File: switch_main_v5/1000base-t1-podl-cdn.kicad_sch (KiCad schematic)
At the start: 11 parts, among them T1901 74930100

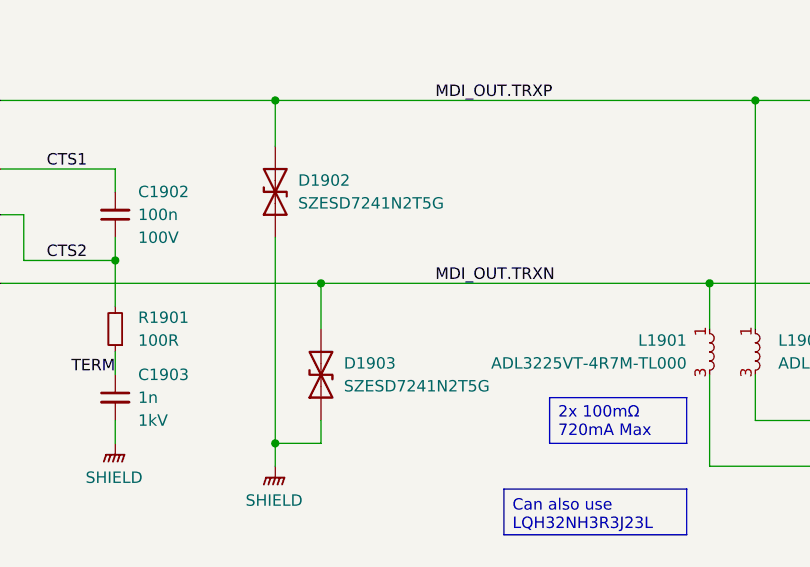
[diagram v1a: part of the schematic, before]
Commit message: Changed main 3V3 regulator to 3A, added switch 2 crystal & other changes
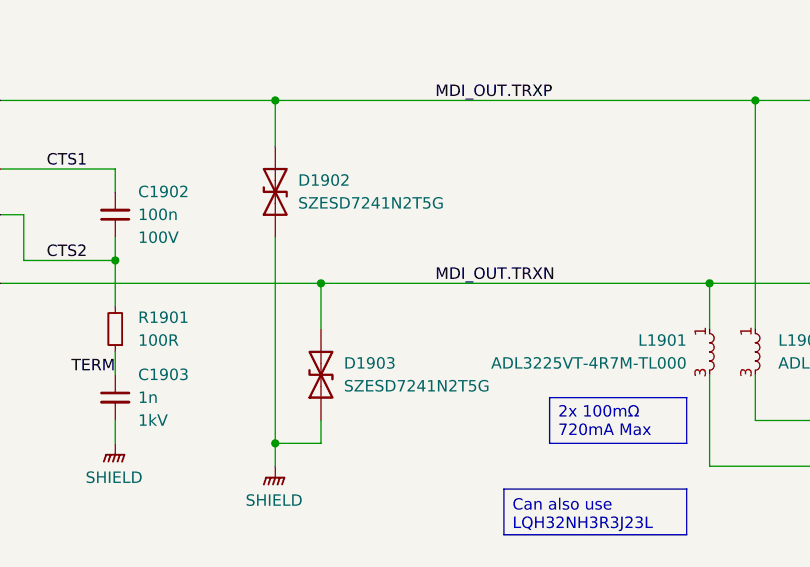
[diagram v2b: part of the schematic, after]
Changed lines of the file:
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@@
 	(symbol
 		(lib_id "TVS:SZESD7241N2T5G")
-		(at 177.8 124.46 90)
+		(at 180.34 124.46 90)
 		(unit 1)
 		(exclude_from_sim no)
@@
 		(on_board yes)
 		(dnp no)
-		(fields_autoplaced yes)
 		(property "Reference" "D1903"
-			(at 182.88 123.1899 90)
+			(at 182.88 123.19 90)
 			(effects
 				(font
@@
 		)
 		(property "Value" "SZESD7241N2T5G"
-			(at 182.88 125.7299 90)
+			(at 182.88 125.73 90)
 			(effects
 				(font
@@
 		)
 		(property "Footprint" "project_footprints:SZESD7462N2T5G"
-			(at 187.96 140.97 0)
+			(at 190.5 140.97 0)
 			(effects
 				(font
@@
 		)
 		(property "Datasheet" "https://www.onsemi.com/pub/Collateral/ESD7241-D.PDF"
-			(at 190.5 153.67 0)
+			(at 193.04 153.67 0)
 			(effects
 				(font
@@
 		)
 		(property "Description" "SZESD7241MXWT5G Wettable Flank Package; SZ Prefix for Automotive and Other Applications Requiring Unique Site and Control Change Requirements; AECQ101 Qualified and PPAP CapableSZ Prefix for Automotive and Other Applications Requiring Unique Site and Control Change Requirements; AECQ101 Qualified and PPAP Capable; Ultra-Low Capacitance: < 1.0pF Max; Low Leakage: < 0.5uA; IEC61000-4-2 (ESD): Level 4 +/-28kV Contact; IEC61000-4-4 (EFT): 40A - 5/50ns; IEC61000-4-5 (Lightning): 1A - 8/20us; These Devices are Pb"
-			(at 184.15 124.46 0)
+			(at 186.69 124.46 0)
 			(effects
 				(font
@@
 		)
 		(property "Height" "0.4"
-			(at 193.04 125.73 0)
+			(at 195.58 125.73 0)
 			(effects
 				(font
@@
 		)
 		(property "Mouser Part Number" "863-SZESD7241N2T5G"
-			(at 195.58 135.89 0)
+			(at 198.12 135.89 0)
 			(effects
 				(font
@@
 		)
 		(property "Mouser Price/Stock" "https://www.mouser.co.uk/ProductDetail/onsemi/SZESD7241N2T5G?qs=z6PAvqrnkvSq0oMCl81g4Q%3D%3D"
-			(at 198.12 173.99 0)
+			(at 200.66 173.99 0)
 			(effects
 				(font
@@
 		)
 		(property "Manufacturer_Name" "onsemi"
-			(at 200.66 128.27 0)
+			(at 203.2 128.27 0)
 			(effects
 				(font
@@
 		)
 		(property "Manufacturer_Part_Number" "SZESD7241N2T5G"
-			(at 203.2 133.35 0)
+			(at 205.74 133.35 0)
 			(effects
 				(font
@@
 	(symbol
 		(lib_id "TVS:SZESD7241N2T5G")
-		(at 172.72 104.14 90)
+		(at 175.26 104.14 90)
 		(unit 1)
 		(exclude_from_sim no)
@@
 		(dnp no)
 		(property "Reference" "D1902"
-			(at 177.8 102.8699 90)
+			(at 177.8 102.87 90)
 			(effects
 				(font
@@
 		)
 		(property "Value" "SZESD7241N2T5G"
-			(at 177.8 105.4099 90)
+			(at 177.8 105.41 90)
 			(effects
 				(font
@@
 		)
 		(property "Footprint" "project_footprints:SZESD7462N2T5G"
-			(at 182.88 120.65 0)
+			(at 185.42 120.65 0)
 			(effects
 				(font
@@
 		)
 		(property "Datasheet" "https://www.onsemi.com/pub/Collateral/ESD7241-D.PDF"
-			(at 185.42 133.35 0)
+			(at 187.96 133.35 0)
 			(effects
 				(font
@@
 		)
 		(property "Description" "SZESD7241MXWT5G Wettable Flank Package; SZ Prefix for Automotive and Other Applications Requiring Unique Site and Control Change Requirements; AECQ101 Qualified and PPAP CapableSZ Prefix for Automotive and Other Applications Requiring Unique Site and Control Change Requirements; AECQ101 Qualified and PPAP Capable; Ultra-Low Capacitance: < 1.0pF Max; Low Leakage: < 0.5uA; IEC61000-4-2 (ESD): Level 4 +/-28kV Contact; IEC61000-4-4 (EFT): 40A - 5/50ns; IEC61000-4-5 (Lightning): 1A - 8/20us; These Devices are Pb"
-			(at 179.07 104.14 0)
+			(at 181.61 104.14 0)
 			(effects
 				(font
@@
 		)
 		(property "Height" "0.4"
-			(at 187.96 105.41 0)
+			(at 190.5 105.41 0)
 			(effects
 				(font
@@
 		)
 		(property "Mouser Part Number" "863-SZESD7241N2T5G"
-			(at 190.5 115.57 0)
+			(at 193.04 115.57 0)
 			(effects
 				(font
@@
 		)
 		(property "Mouser Price/Stock" "https://www.mouser.co.uk/ProductDetail/onsemi/SZESD7241N2T5G?qs=z6PAvqrnkvSq0oMCl81g4Q%3D%3D"
-			(at 193.04 153.67 0)
+			(at 195.58 153.67 0)
 			(effects
 				(font
@@
 		)
 		(property "Manufacturer_Name" "onsemi"
-			(at 195.58 107.95 0)
+			(at 198.12 107.95 0)
 			(effects
 				(font
@@
 		)
 		(property "Manufacturer_Part_Number" "SZESD7241N2T5G"
-			(at 198.12 113.03 0)
-			(effects
-				(font
+			(at 200.66 113.03 0)
+			(effects
+				(font

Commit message: Tidied schematic and PCB
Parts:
- renumbered C1902 to C2701, C1901 to C2702, C1903 to C2703, D1902 to D2701, D1901 to D2702, D1903 to D2703, FL1901 to FL2701, L1901 to L2701, L1902 to L2702, R1901 to R2701, T1901 to T2701
